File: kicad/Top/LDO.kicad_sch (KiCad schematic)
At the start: 8 parts

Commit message: Properly synced pcb to schematic
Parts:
- C42, C43: value ~ -> GRM155R61E104KA87D; footprint 0402L -> AltiumImports:0402L
- D11, D12: value ~ -> BAT54HT1G; footprint SOD-323 -> AltiumImports:SOD-323
- JP32: value ~ -> Header_2x1; footprint CONN_PEC02SAAN -> AltiumImports:CONN_PEC02SAAN
- R37: value ~ -> ERJ-8ENF10R0V; footprint 1206 -> AltiumImports:1206
- R38: value ~ -> 5106; footprint 5106 -> AltiumImports:5106
- U2: value ~ -> TLV76033DBZR; footprint DBZ0003A_N -> AltiumImports:DBZ0003A_N
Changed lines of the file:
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@@
       (effects (font (size 1.27 1.27)) (justify left bottom))
     )
-    (property "Value" "~" (id 1) (at 156.21 120.65 0)
-      (effects (font (size 1.27 1.27)) (justify left bottom) hide)
-    )
-    (property "Footprint" "5106" (id 2) (at 157.48 116.84 0)
+    (property "Value" "5106" (id 1) (at 156.21 120.65 0)
+      (effects (font (size 1.27 1.27)) (justify left bottom) hide)
+    )
+    (property "Footprint" "AltiumImports:5106" (id 2) (at 157.48 116.84 0)
       (effects (font (size 1.27 1.27)) hide)
     )
@@
   (symbol (lib_id "Top-altium-import:3V3_U2") (at 124.46 68.58 90) (unit 1)
     (in_bom yes) (on_board yes)
-    (property "Reference" "#PWR?" (id 0) (at 124.46 68.58 0)
+    (property "Reference" "#PWR0253" (id 0) (at 124.46 68.58 0)
       (effects (font (size 1.27 1.27)) hide)
     )
@@
       (effects (font (size 1.27 1.27)) (justify left bottom))
     )
-    (property "Value" "~" (id 1) (at 76.454 96.266 0)
-      (effects (font (size 1.27 1.27)) (justify left bottom) hide)
-    )
-    (property "Footprint" "SOD-323" (id 2) (at 73.66 93.98 0)
+    (property "Value" "BAT54HT1G" (id 1) (at 76.454 96.266 0)
+      (effects (font (size 1.27 1.27)) (justify left bottom) hide)
+    )
+    (property "Footprint" "AltiumImports:SOD-323" (id 2) (at 73.66 93.98 0)
       (effects (font (size 1.27 1.27)) hide)
     )
@@
       (effects (font (size 1.27 1.27)) (justify left bottom))
     )
-    (property "Value" "~" (id 1) (at 68.58 116.332 0)
-      (effects (font (size 1.27 1.27)) (justify left bottom) hide)
-    )
-    (property "Footprint" "CONN_PEC02SAAN" (id 2) (at 71.12 121.92 0)
+    (property "Value" "Header_2x1" (id 1) (at 68.58 116.332 0)
+      (effects (font (size 1.27 1.27)) (justify left bottom) hide)
+    )
+    (property "Footprint" "AltiumImports:CONN_PEC02SAAN" (id 2) (at 71.12 121.92 0)
       (effects (font (size 1.27 1.27)) hide)
     )
@@
   (symbol (lib_id "Top-altium-import:BAT_U1") (at 71.12 81.28 270) (unit 1)
     (in_bom yes) (on_board yes)
-    (property "Reference" "#PWR?" (id 0) (at 71.12 81.28 0)
+    (property "Reference" "#PWR0255" (id 0) (at 71.12 81.28 0)
       (effects (font (size 1.27 1.27)) hide)
     )
@@
   (symbol (lib_id "Top-altium-import:PGND") (at 64.77 58.42 0) (unit 1)
     (in_bom yes) (on_board yes)
-    (property "Reference" "#PWR?" (id 0) (at 64.77 58.42 0)
+    (property "Reference" "#PWR0256" (id 0) (at 64.77 58.42 0)
       (effects (font (size 1.27 1.27)) hide)
     )
@@
   (symbol (lib_id "Top-altium-import:PGND") (at 175.26 129.54 0) (unit 1)
     (in_bom yes) (on_board yes)
-    (property "Reference" "#PWR?" (id 0) (at 175.26 129.54 0)
+    (property "Reference" "#PWR0258" (id 0) (at 175.26 129.54 0)
       (effects (font (size 1.27 1.27)) hide)
     )
@@
   (symbol (lib_id "Top-altium-import:PGND") (at 99.06 129.54 0) (unit 1)
     (in_bom yes) (on_board yes)
-    (property "Reference" "#PWR?" (id 0) (at 99.06 129.54 0)
+    (property "Reference" "#PWR0260" (id 0) (at 99.06 129.54 0)
       (effects (font (size 1.27 1.27)) hide)
     )
@@
   (symbol (lib_id "Top-altium-import:VBUS") (at 45.72 81.28 270) (unit 1)
     (in_bom yes) (on_board yes)
-    (property "Reference" "#PWR?" (id 0) (at 45.72 81.28 0)
+    (property "Reference" "#PWR0257" (id 0) (at 45.72 81.28 0)
       (effects (font (size 1.27 1.27)) hide)
     )
@@
   (symbol (lib_id "Top-altium-import:BAT_U1") (at 124.46 53.34 90) (unit 1)
     (in_bom yes) (on_board yes)
-    (property "Reference" "#PWR?" (id 0) (at 124.46 53.34 0)
+    (property "Reference" "#PWR0252" (id 0) (at 124.46 53.34 0)
       (effects (font (size 1.27 1.27)) hide)
     )
@@
       (effects (font (size 1.27 1.27)) (justify left bottom))
     )
-    (property "Value" "~" (id 1) (at 242.57 -21.59 0)
-      (effects (font (size 1.27 1.27)) (justify left bottom) hide)
-    )
-    (property "Footprint" "DBZ0003A_N" (id 2) (at 127 119.38 0)
+    (property "Value" "TLV76033DBZR" (id 1) (at 242.57 -21.59 0)
+      (effects (font (size 1.27 1.27)) (justify left bottom) hide)
+    )
+    (property "Footprint" "AltiumImports:DBZ0003A_N" (id 2) (at 127 119.38 0)
       (effects (font (size 1.27 1.27)) hide)
     )
@@
   (symbol (lib_id "Top-altium-import:3V3_U2") (at 187.96 116.84 90) (unit 1)
     (in_bom yes) (on_board yes)
-    (property "Reference" "#PWR?" (id 0) (at 187.96 116.84 0)
+    (property "Reference" "#PWR0259" (id 0) (at 187.96 116.84 0)
       (effects (font (size 1.27 1.27)) hide)
     )
@@
       (effects (font (size 1.27 1.27)) (justify left bottom))
     )
-    (property "Value" "~" (id 1) (at 51.054 96.266 0)
-      (effects (font (size 1.27 1.27)) (justify left bottom) hide)
-    )
-    (property "Footprint" "SOD-323" (id 2) (at 48.26 93.98 0)
+    (property "Value" "BAT54HT1G" (id 1) (at 51.054 96.266 0)
+      (effects (font (size 1.27 1.27)) (justify left bottom) hide)
+    )
+    (property "Footprint" "AltiumImports:SOD-323" (id 2) (at 48.26 93.98 0)
       (effects (font (size 1.27 1.27)) hide)
     )
@@
       (effects (font (size 1.27 1.27)) (justify left bottom))
     )
-    (property "Value" "~" (id 1) (at 172.974 118.872 0)
-      (effects (font (size 1.27 1.27)) (justify left bottom) hide)
-    )
-    (property "Footprint" "0402L" (id 2) (at 175.26 121.92 0)
+    (property "Value" "GRM155R61E104KA87D" (id 1) (at 172.974 118.872 0)
+      (effects (font (size 1.27 1.27)) (justify left bottom) hide)
+    )
+    (property "Footprint" "AltiumImports:0402L" (id 2) (at 175.26 121.92 0)
       (effects (font (size 1.27 1.27)) hide)
     )
@@
       (effects (font (size 1.27 1.27)) (justify left bottom))
     )
-    (property "Value" "~" (id 1) (at 85.09 120.65 0)
-      (effects (font (size 1.27 1.27)) (justify left bottom) hide)
-    )
-    (property "Footprint" "1206" (id 2) (at 86.36 116.84 0)
+    (property "Value" "ERJ-8ENF10R0V" (id 1) (at 85.09 120.65 0)
+      (effects (font (size 1.27 1.27)) (justify left bottom) hide)
+    )
+    (property "Footprint" "AltiumImports:1206" (id 2) (at 86.36 116.84 0)
       (effects (font (size 1.27 1.27)) hide)
     )
@@
       (effects (font (size 1.27 1.27)) (justify left bottom))
     )
-    (property "Value" "~" (id 1) (at 96.774 118.872 0)
-      (effects (font (size 1.27 1.27)) (justify left bottom) hide)
-    )
-    (property "Footprint" "0402L" (id 2) (at 99.06 121.92 0)
+    (property "Value" "GRM155R61E104KA87D" (id 1) (at 96.774 118.872 0)
+      (effects (font (size 1.27 1.27)) (justify left bottom) hide)
+    )
+    (property "Footprint" "AltiumImports:0402L" (id 2) (at 99.06 121.92 0)
       (effects (font (size 1.27 1.27)) hide)
     )
@@
   (symbol (lib_id "Top-altium-import:VBUS") (at 124.46 60.96 90) (unit 1)
     (in_bom yes) (on_board yes)
-    (property "Reference" "#PWR?" (id 0) (at 124.46 60.96 0)
-      (effects (font (size 1.27 1.27)) hide)
-    )
+    (property "Reference" "#PWR0254" (id 0) (at 124.46 60.96 0)
+      (effects (font (size 1.27 1.27)) hide)
+    )

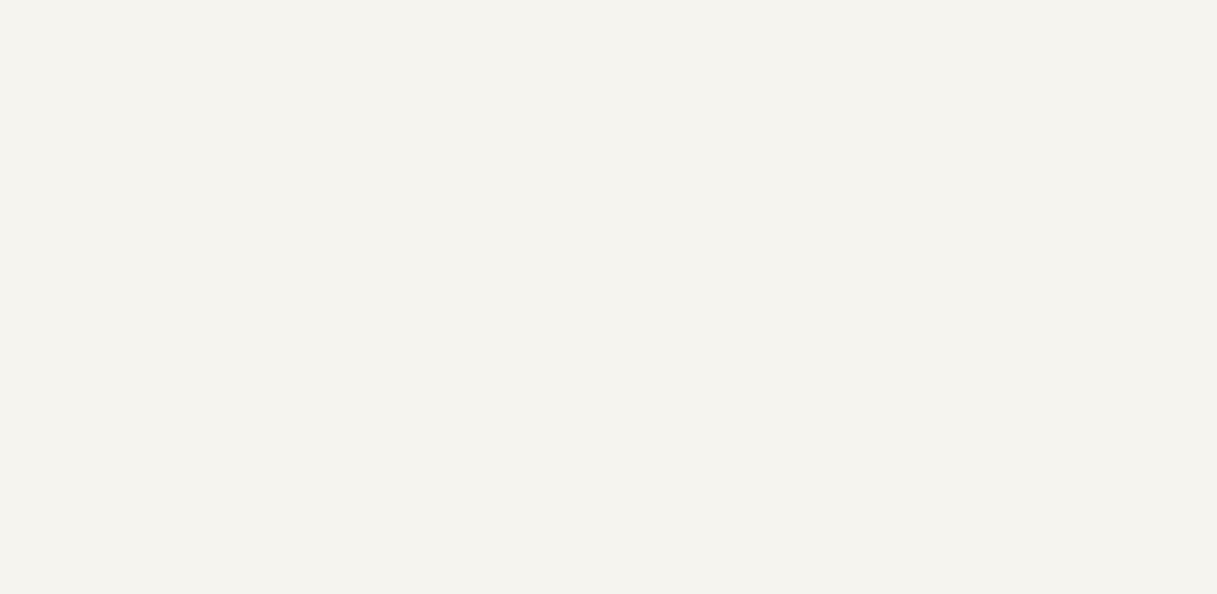
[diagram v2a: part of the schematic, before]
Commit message: Merged LDOs and moved to top sheet
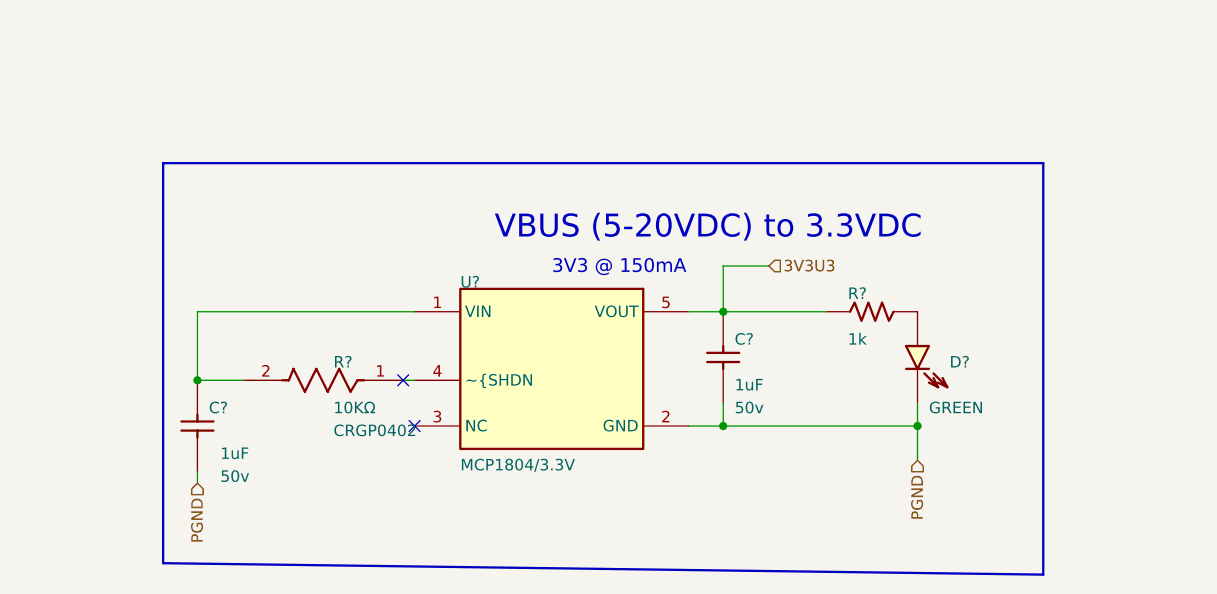
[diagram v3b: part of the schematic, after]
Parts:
- added C? (x2): Capacitor NP, AltiumImports:_ALTIUM_WORK_00001_MCHP-CDB_Library_Database_.._Footprints_CAP_C_0603.PcbLib_CAP_C_0603, symbol Top-altium-import:1_Capacitor NP
- added D?: LED_green, AltiumImports:_ALTIUM_WORK_00001_MCHP-CDB_Library_Database_.._Footprints_LED_0603_Green.PcbLib_LED_0603_GREEN, symbol Top-altium-import:3_LED_green
- added R?: CRGP0402F10K, AltiumImports:FP-CRGP0402-IPC_A, symbol Top-altium-import:2_CMP-03211-008310-1
- added R?: Resistor, AltiumImports:_ALTIUM_WORK_00001_MCHP-CDB_Library_Database_MCHP-CDB.DbLib_Resistor_RES_C_0402, symbol Top-altium-import:2_Resistor
- added U?: MCP1804 SOT-23-5, AltiumImports:_ALTIUM_WORK_00001_MCHP-CDB_Library_Database_MCHP-CDB.DbLib_MCHP-Analog_SOT-23-5, symbol Top-altium-import:0_MCP1804 SOT-23-5
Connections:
- net PGND: now also C?.1, C?.1, D?.2 (K), U?.2 (GND)
- new net: D?.1 (A), R?.1
- new net: R?.1, U?.4 (~{SHDN)
- new net: C?.2, R?.2, U?.1 (VIN)
- new net 3V3U3: C?.2, R?.2, U?.5 (VOUT)
- no-connect marks 0 -> 2
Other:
- note added: "3V3 @ 150mA"
- note added: "VBUS (5-20VDC) to 3.3VDC"
